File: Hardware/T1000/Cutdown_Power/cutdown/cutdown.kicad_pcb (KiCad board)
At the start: 4 copper layers, 48 x 32 mm, 35 parts, among them J2 Conn_01x06_Socket, J3 Conn_01x01_Pin, J4 Conn_01x01_Pin, Q1 NMOS, Q2 NMOS, U1 LTC1751, U2 LTC7061IMSE-WTRPBF

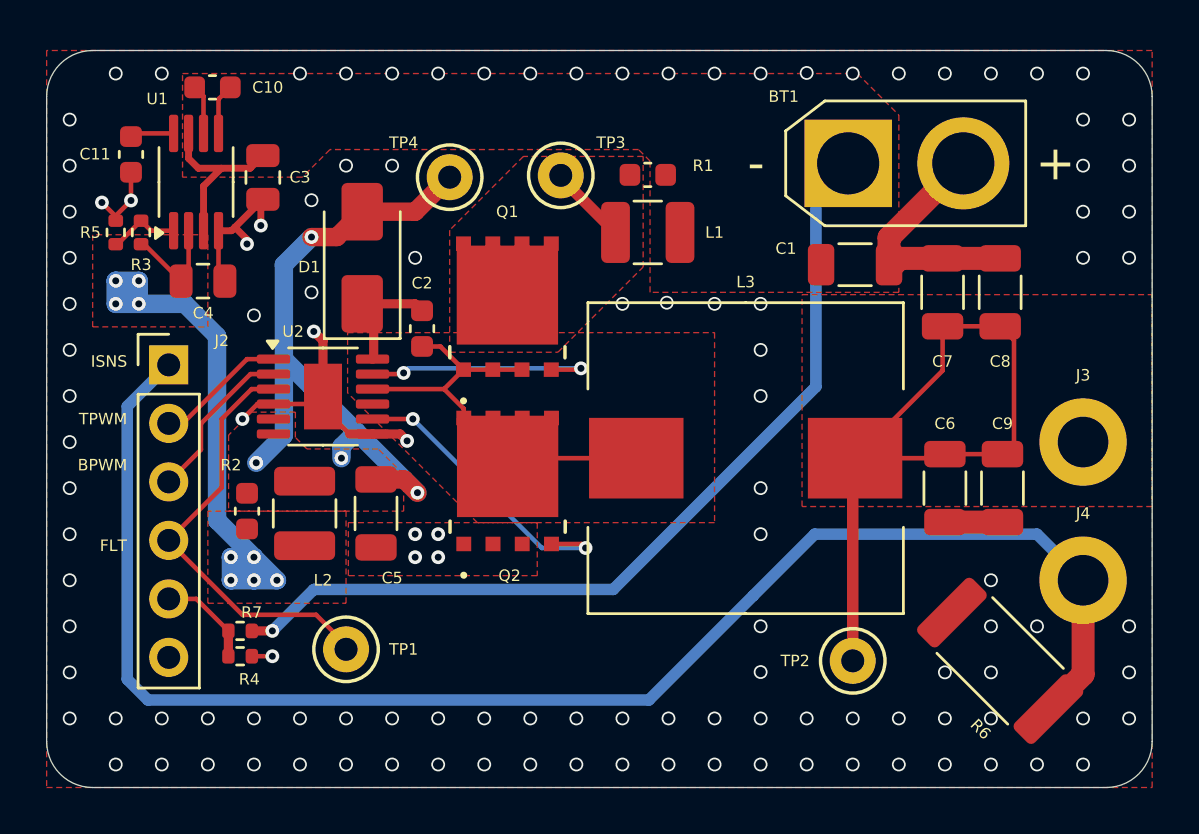
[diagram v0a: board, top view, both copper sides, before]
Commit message: V0.1 of cutdown board to add opamp scaling on current sense
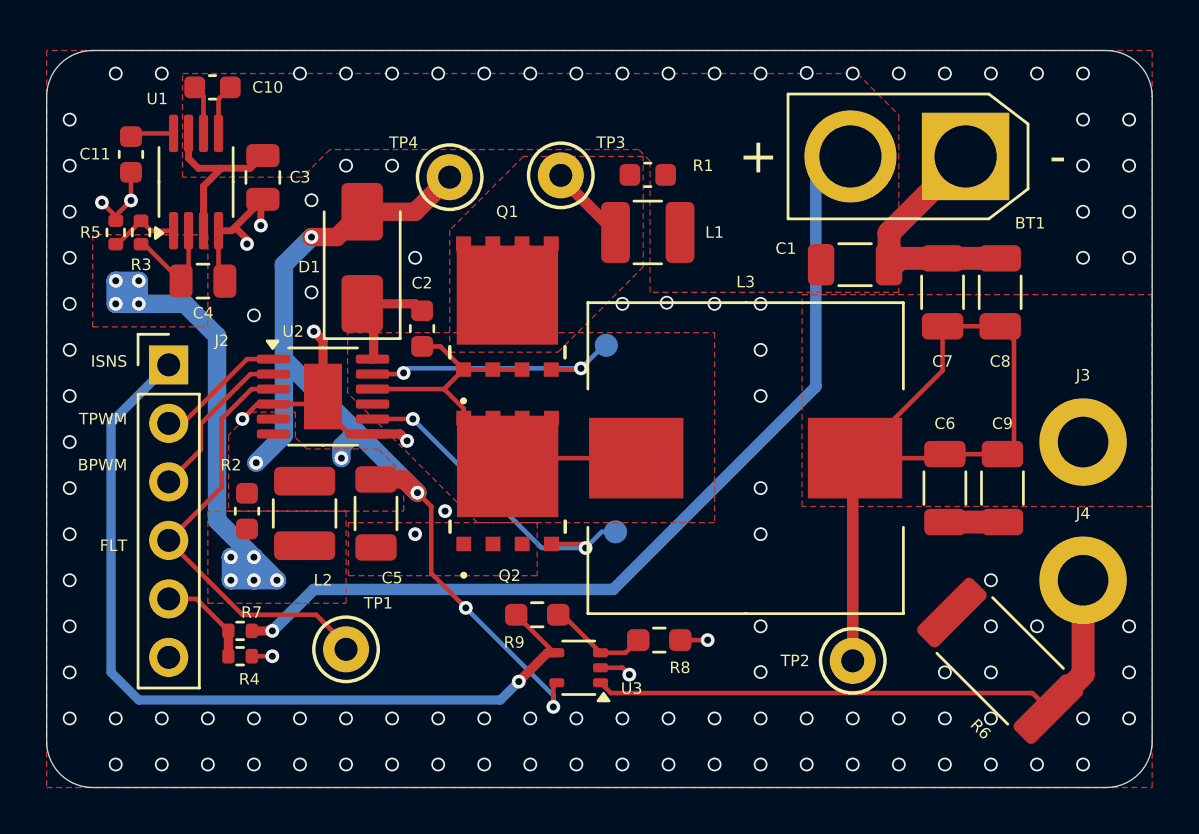
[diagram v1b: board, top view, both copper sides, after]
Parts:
- added R8: 1.4k, Resistor_SMD:R_0603_1608Metric_Pad0.98x0.95mm_HandSolder, F.Cu at (141.6, 113.6)
- added R9: 39.2k, Resistor_SMD:R_0603_1608Metric_Pad0.98x0.95mm_HandSolder, F.Cu at (136.3, 112.5)
- added TP5: TestPoint, TestPoint:TestPoint_Pad_D1.0mm, B.Cu at (139.3, 100.8)
- added TP6: TestPoint, TestPoint:TestPoint_Pad_D1.0mm, B.Cu at (139.7, 108.9)
- added U3: TLV172IDCK, Package_TO_SOT_SMD:SOT-353_SC-70-5, F.Cu at (138.1, 114.8)
- C2: value C_Small -> 100nF
- moved BT1 5.11 mm to (154.9, 92.6), turned to 180 degrees
- moved REF** 4.80 mm to (131.2, 114.2)
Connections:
- net Net-(D1-A) renamed VCC
- BT1 pad 1: +BATT -> GND
- BT1 pad 2: GND -> +BATT
- J4 pad 1: /ISNS -> Net-(J4-Pin_1)
- R6 pad 2: /ISNS -> Net-(J4-Pin_1)
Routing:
- net /ISNS: track 66.4 -> 37.6 mm, vias 0 -> 1
- net Net-(J4-Pin_1): track 0.00 -> 26.1 mm
- net VCC: track 29.5 -> 42.4 mm, vias 4 -> 6
- net Net-(U3--): track 0.00 -> 4.39 mm
- net GND: track 36.0 -> 38.9 mm
- net Net-(Q2-G): track 13.1 -> 14.7 mm
- net Net-(Q1-G): track 10.5 -> 12.0 mm
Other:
- board text added: "Michael Shipman V0.1 10/28/2024"
- board text removed: "Michael Shipman V0.0 9/11/2024"

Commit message: cutdown power stage V1.0 changes
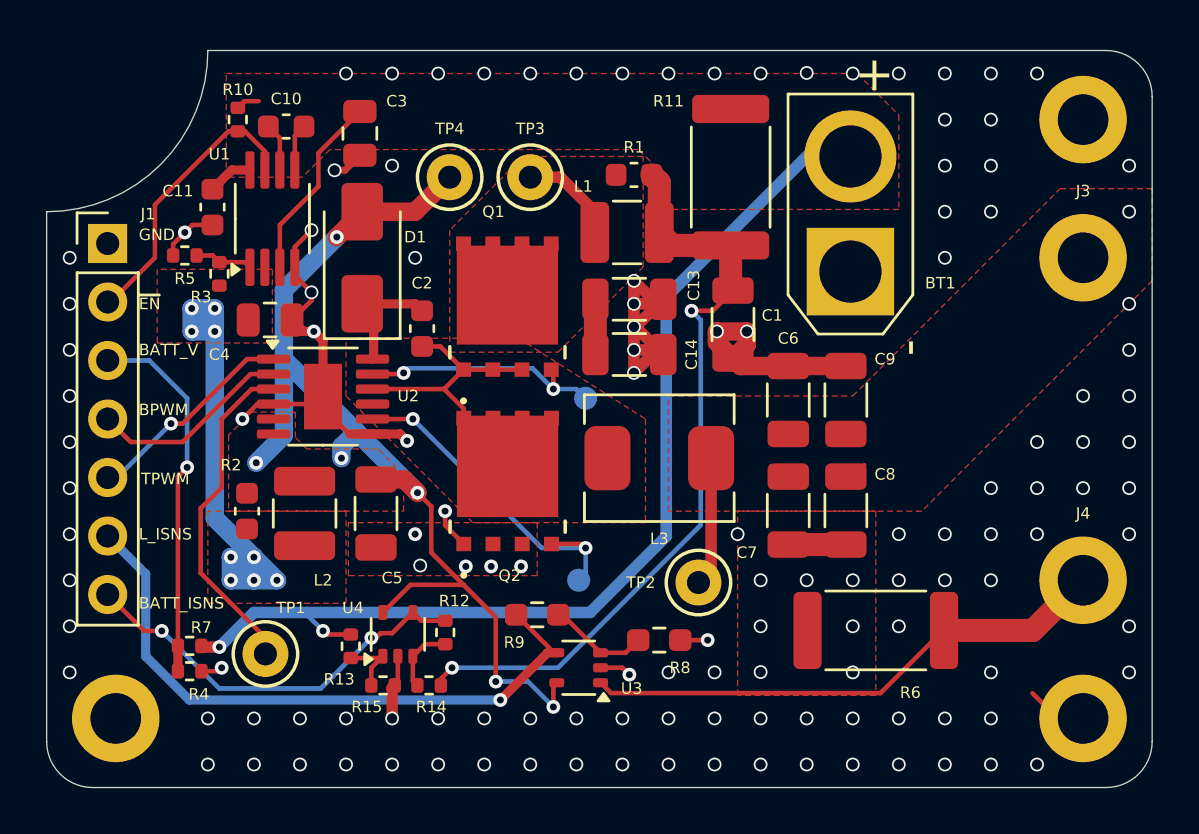
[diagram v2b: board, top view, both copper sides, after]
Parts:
- removed J2: Conn_01x06_Socket, Connector_PinHeader_2.54mm:PinHeader_1x06_P2.54mm_Vertical
- added C13: 10uF, Capacitor_SMD:C_1206_3216Metric, F.Cu at (140.3, 98.8)
- added C14: 10uF, Capacitor_SMD:C_1206_3216Metric, F.Cu at (140.3, 101.2)
- added H2: MountingHole_Pad, MountingHole:MountingHole_2.2mm_M2_DIN965_Pad, F.Cu at (118.0, 117.0)
- added H3: MountingHole_Pad, MountingHole:MountingHole_2.2mm_M2_DIN965_Pad, F.Cu at (160.0, 91.0)
- added H4: MountingHole_Pad, MountingHole:MountingHole_2.2mm_M2_DIN965_Pad, F.Cu at (160.0, 117.0)
- added J1: Conn_01x07_Socket, BPP_Lib:Molex_ 1718570007, F.Cu at (117.7, 96.4)
- added R10: 10k, Resistor_SMD:R_0402_1005Metric, F.Cu at (123.3, 91.0)
- added R11: 5m, Resistor_SMD:R_2512_6332Metric, F.Cu at (144.7, 93.5)
- added R12: 30k, Resistor_SMD:R_0402_1005Metric, F.Cu at (132.3, 113.3)
- added R13: 1k, Resistor_SMD:R_0402_1005Metric, F.Cu at (128.2, 113.9)
- added R14: 1k, Resistor_SMD:R_0402_1005Metric, F.Cu at (131.6, 115.6)
- added R15: 30k, Resistor_SMD:R_0402_1005Metric, F.Cu at (129.6, 115.6)
- added U4: TLV172IDCK, Package_TO_SOT_SMD:SOT-353_SC-70-5, F.Cu at (130.2, 113.3)
- L3: footprint BPP_Lib:Wurth_74437368047 -> BPP_Lib:IHLP2020CZER1R5M8A
- REF**: moved to B.Cu
- moved REF** 28.4 mm to (156.4, 101.2), turned to 180 degrees
- moved C7 8.17 mm to (147.2, 103.2)
- moved C8 8.17 mm to (149.7, 103.2)
- moved J3 8.00 mm to (160.0, 97.0)
- moved TP2 7.51 mm to (143.3, 111.1)
- moved BT1 7.07 mm to (149.9, 97.6), turned to 90 degrees
- moved C6 6.87 mm to (147.2, 108.0)
- moved C9 6.87 mm to (149.7, 108.0)
- moved C1 5.90 mm to (144.8, 99.9), turned to -90 degrees
- moved R6 5.56 mm to (151.0, 113.2), turned to 0 degrees
- moved C3 4.63 mm to (128.6, 91.6)
- moved C11 4.21 mm to (122.2, 94.8)
- moved R3 3.85 mm to (122.5, 97.7)
- moved L3 3.75 mm to (141.6, 105.7), turned to 180 degrees
- moved U1 3.67 mm to (124.8, 95.3)
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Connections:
- net /COMP2_INP renamed /BATT_V
- net /FLT renamed Net-(U2-~{FLT})
- net /ISNS renamed /LOAD_ISNS
- C1 pad 1: +BATT -> Net-(C1-Pad1)
- L1 pad 2: +BATT -> Net-(C1-Pad1)
- R1 pad 2: +BATT -> Net-(C1-Pad1)
- U1 pad 7: +BATT -> /~{EN}
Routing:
- net Net-(C1-Pad1): track 0.00 -> 33.9 mm, vias 0 -> 2
- net Net-(J3-Pin_1): track 31.1 -> 6.58 mm
- net /BATT_ISNS: track 0.00 -> 17.9 mm, vias 0 -> 2
- net GND: track 38.9 -> 55.7 mm, vias 121 -> 130
- net /~{EN}: track 0.00 -> 12.4 mm
- net /BATT_V: track 4.27 -> 16.1 mm, vias 0 -> 1
- net /LOAD_ISNS: track 37.6 -> 27.8 mm
- net Net-(U1-VOUT): track 33.6 -> 25.2 mm
- net +BATT: track 47.0 -> 53.4 mm, vias 1 -> 2
- net Net-(Q1-S): track 20.2 -> 15.1 mm
- net Net-(U2-~{FLT}): track 18.8 -> 14.5 mm
- net VCC: track 42.4 -> 46.6 mm
- net /TOP_PWM: track 5.97 -> 9.33 mm, vias 0 -> 1
- net Net-(Q1-D): track 3.46 -> 6.72 mm
- net Net-(J4-Pin_1): track 26.1 -> 23.2 mm
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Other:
- outline, holes or cut-outs redrawn
- board text added: "BATT_ISNS"
- board text added: "BATT_V"
- board text added: "GND"
- board text added: "L_ISNS"
- board text added: "Michael Shipman V1.0 02/13/2025"
- board text added: "~{EN}"
- board text removed: "FLT"
- board text removed: "ISNS"
- board text removed: "Michael Shipman V0.1 10/28/2024"
